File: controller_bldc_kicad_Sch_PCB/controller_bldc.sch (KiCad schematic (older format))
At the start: 75 parts, among them J1 Battery Supply, J4 Brake, J5 Throttle, J6 LM35, J7 Hall Sensors, J8 Nextion Nx3224T028, J9 BLDC Motor, K1 RAYEX-L90B, Q1 IRF1010N, Q2 IRF1010N, Q3 IRF1010N, Q4 IRF1010N, Q5 IRF1010N, Q6 IRF1010N, Q7 PN2222A, SW1 ON_OFF, SW2 OPC, U1 ESP32-DEVKITC-32D, U2 MC1458P, U3 LM2596SOURCE_Pin2, U4 IR2103, U5 LM2596SOURCE, U8 IR2103, U9 IR2103

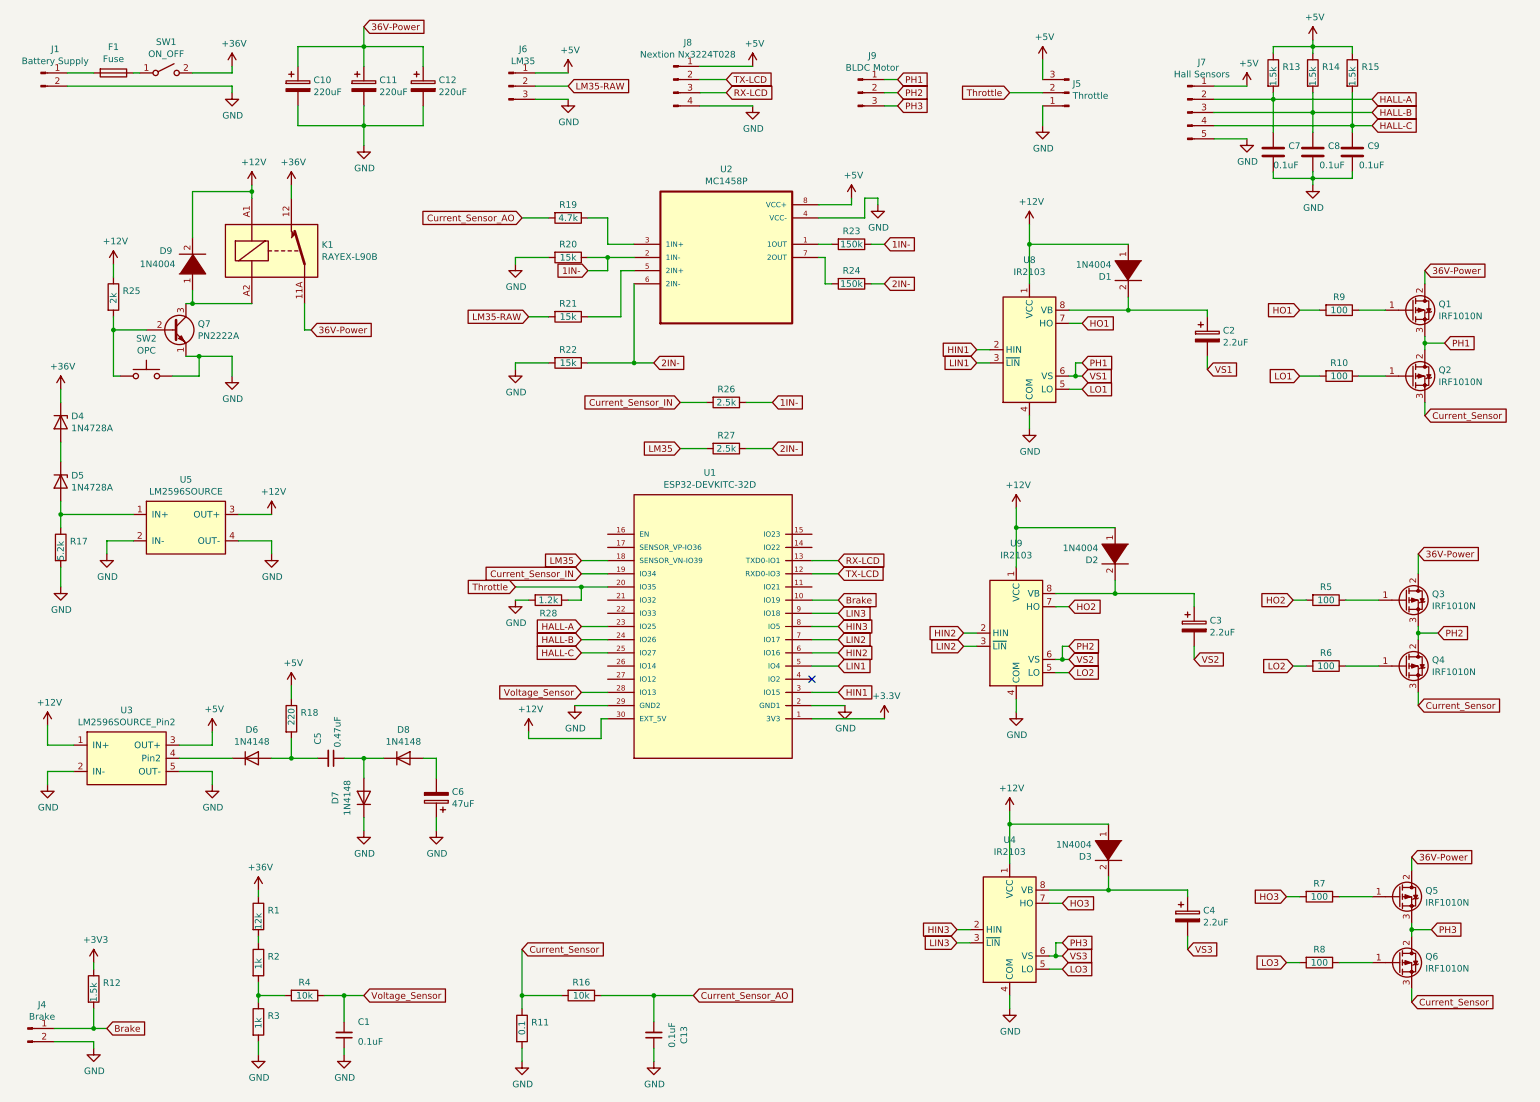
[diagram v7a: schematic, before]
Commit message: PCB Finished, this is version 2.0. Closes #9 and closes #10.
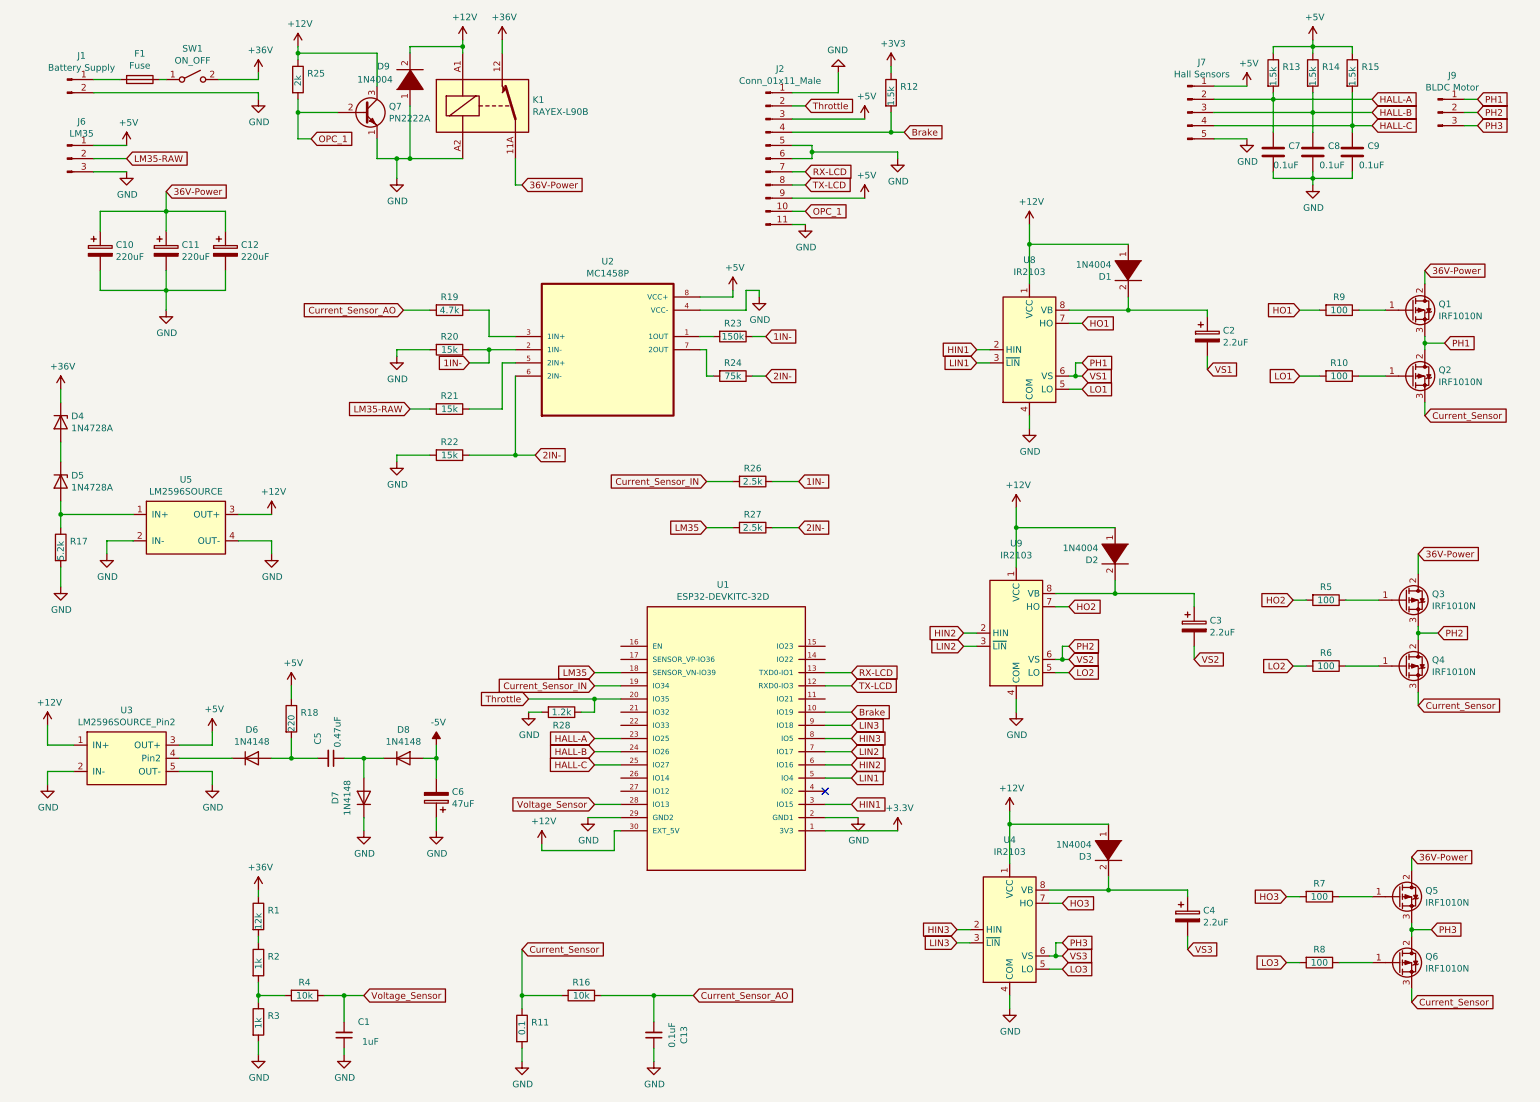
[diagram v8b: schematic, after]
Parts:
- removed J4: Brake, Connector_Molex:Molex_KK-254_AE-6410-02A_1x02_P2.54mm_Vertical, symbol Connector:Conn_01x02_Male
- removed J5: Throttle, Connector_Molex:Molex_KK-254_AE-6410-03A_1x03_P2.54mm_Vertical, symbol Connector:Conn_01x03_Male
- removed J8: Nextion Nx3224T028, Connector_Molex:Molex_KK-254_AE-6410-04A_1x04_P2.54mm_Vertical, symbol Connector:Conn_01x04_Male
- removed SW2: OPC, Connector_Molex:Molex_KK-254_AE-6410-02A_1x02_P2.54mm_Vertical, symbol Switch:SW_Push
- added J2: Conn_01x11_Male, Connector_Molex:Molex_KK-254_AE-6410-11A_1x11_P2.54mm_Vertical, symbol Connector:Conn_01x11_Male
- C1: value 0.1uF -> 1uF
- R24: value 150k -> 75k
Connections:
- net +12V: now also Q7.3 (C)
- net +5V: now also J2.3 (Pin_3), J2.9 (Pin_9)
- net Brake: now also J2.4 (Pin_4)
- net GND: now also D9.1 (K), K1.A2, J2.1 (Pin_1), J2.11 (Pin_11), J2.5 (Pin_5), J2.6 (Pin_6)
- net RX-LCD: now also J2.7 (Pin_7)
- net TX-LCD: now also J2.8 (Pin_8)
- net Throttle: now also J2.2 (Pin_2)
- net -5V: now reaches C6.2, D8.2 (A)
- net OPC_1: now reaches Q7.2 (B), R25.2
- net OPC_1: now also J2.10 (Pin_10)
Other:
- moved on the sheet: C10, C11, C12, D9, F1, J1, J6, J9, K1, Q7, R12, R19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
